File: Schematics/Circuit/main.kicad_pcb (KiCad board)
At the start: 2 copper layers, 59.3 x 59 mm, 93 parts, among them IC1 NCP1117ST33T3G, IC2 NCP1117ST50T3G, IC3 ATMEGA2560-A, IC4 RFM69HW, J1 Conn_01x03, J10 Conn_01x04, J2 Conn_01x07, J3 Conn_01x07, J4 Conn_01x07, J5 Conn_01x07, J6 Conn_01x07, J7 Conn_01x05, J8 Conn_02x05_Counter_Clockwise, J9 Conn_01x06, K1 HESOP1, K2 HESOP1, P1 CONN_2, P10 CONN_2, P11 CONN_2, P12 CONN_2, P13 CONN_2, P14 CONN_2, P15 CONN_2, P16 CONN_2, P17 CONN_2, P18 CONN_3X2, P19 CONN_O2, P2 CONN_2, P20 CONN_2, P21 CONN_2, P3 CONN_2, P4 CONN_2, P5 CONN_2, P6 CONN_2, P7 CONN_2, P8 CONN_2, P9 CONN_2, Q1 BSS138, Q2 BSS138, Q3 BSS138, Q4 BSS138, Q5 BSS138, Q6 BSS138

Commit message: Edit pcb and model
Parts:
- added J11: Conn_01x04, CanSat:MOLEX_PicoBlade_4, F.Cu at (245.9, 86.1)
- moved R15 0.42 mm to (250.7, 97.4)
- moved R24 0.15 mm to (242.5, 100.1)
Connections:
- IC3 pad 12: /RX -> /TXD-GSM
- IC3 pad 13: /TX -> /RXD-GSM
- IC3 pad 2: /TXD-GSM -> /RX
- IC3 pad 27: (no net) -> Net-(IC3-Pad27)
- IC3 pad 28: (no net) -> Net-(IC3-Pad28)
- IC3 pad 29: (no net) -> Net-(IC3-Pad29)
- IC3 pad 3: /RXD-GSM -> /TX
- IC3 pad 35: (no net) -> Net-(IC3-Pad35)
- IC3 pad 36: (no net) -> Net-(IC3-Pad36)
- IC3 pad 4: (no net) -> Net-(IC3-Pad4)
- IC3 pad 41: (no net) -> Net-(IC3-Pad41)
- IC3 pad 42: (no net) -> Net-(IC3-Pad42)
- IC3 pad 46: (no net) -> Net-(IC3-Pad46)
- IC3 pad 48: (no net) -> Net-(IC3-Pad48)
- IC3 pad 5: (no net) -> Net-(IC3-Pad5)
- IC3 pad 51: (no net) -> Net-(IC3-Pad51)
- IC3 pad 52: (no net) -> Net-(IC3-Pad52)
- IC3 pad 53: (no net) -> Net-(IC3-Pad53)
- IC3 pad 54: (no net) -> Net-(IC3-Pad54)
- IC3 pad 57: (no net) -> Net-(IC3-Pad57)
- IC3 pad 58: (no net) -> Net-(IC3-Pad58)
- IC3 pad 60: (no net) -> Net-(IC3-Pad60)
- IC3 pad 63: (no net) -> /RX_GPS
- IC3 pad 64: (no net) -> /TX_GPS
- IC3 pad 65: (no net) -> Net-(IC3-Pad65)
- IC3 pad 66: (no net) -> Net-(IC3-Pad66)
- IC3 pad 67: (no net) -> Net-(IC3-Pad67)
- IC3 pad 69: (no net) -> Net-(IC3-Pad69)
- IC3 pad 70: (no net) -> Net-(IC3-Pad70)
- IC3 pad 77: (no net) -> Net-(IC3-Pad77)
- IC3 pad 78: (no net) -> Net-(IC3-Pad78)
- IC3 pad 79: (no net) -> Net-(IC3-Pad79)
- IC3 pad 82: (no net) -> Net-(IC3-Pad82)
- IC3 pad 83: (no net) -> Net-(IC3-Pad83)
- IC3 pad 84: (no net) -> Net-(IC3-Pad84)
- IC3 pad 85: (no net) -> Net-(IC3-Pad85)
- IC3 pad 86: (no net) -> Net-(IC3-Pad86)
- IC3 pad 87: (no net) -> Net-(IC3-Pad87)
- IC3 pad 88: (no net) -> Net-(IC3-Pad88)
- IC3 pad 89: (no net) -> Net-(IC3-Pad89)
- IC3 pad 90: (no net) -> Net-(IC3-Pad90)
- IC3 pad 91: (no net) -> Net-(IC3-Pad91)
- IC3 pad 92: (no net) -> Net-(IC3-Pad92)
- IC3 pad 93: (no net) -> Net-(IC3-Pad93)
- IC3 pad 94: (no net) -> Net-(IC3-Pad94)
- IC3 pad 95: (no net) -> Net-(IC3-Pad95)
- IC3 pad 98: (no net) -> Net-(IC3-Pad98)
- IC4 pad 1: (no net) -> Net-(IC4-Pad1)
- IC4 pad 10: (no net) -> Net-(IC4-Pad10)
- IC4 pad 16: (no net) -> Net-(IC4-Pad16)
- IC4 pad 3: (no net) -> Net-(IC4-Pad3)
- IC4 pad 4: (no net) -> Net-(IC4-Pad4)
- IC4 pad 5: (no net) -> Net-(IC4-Pad5)
- IC4 pad 6: (no net) -> Net-(IC4-Pad6)
- IC4 pad 7: (no net) -> Net-(IC4-Pad7)
- J8 pad 1: (no net) -> /DTR
- J8 pad 6: (no net) -> Net-(J8-Pad6)
- K1 pad 3: (no net) -> Net-(K1-Pad3)
- K1 pad 4: (no net) -> Net-(K1-Pad4)
- K2 pad 3: (no net) -> Net-(K2-Pad3)
- K2 pad 4: (no net) -> Net-(K2-Pad4)
- P18 pad 4: (no net) -> Net-(P18-Pad4)
- P19 pad 3: (no net) -> Net-(P19-Pad3)
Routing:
- net +12V: track 605.0 -> 645.1 mm, vias 0 -> 3
- net /RX_GPS: track 0.00 -> 37.5 mm, vias 0 -> 2
- net /TX_GPS: track 0.00 -> 30.4 mm, vias 0 -> 2
- net +5V: track 291.3 -> 311.9 mm, vias 25 -> 28
- net GND: track 806.2 -> 792.4 mm, vias 21 -> 27
- net /TXD-GSM: track 13.4 -> 24.8 mm, vias 0 -> 2
- net Net-(J2-Pad5): track 51.5 -> 42.6 mm, vias 5 -> 3
- net /SCL: track 119.7 -> 126.5 mm, vias 9 -> 10
- net /TX: track 31.8 -> 36.6 mm
- net /LED_TOP: track 25.2 -> 20.9 mm
- net /RX: track 40.9 -> 43.4 mm
- net /RFMINT: track 30.6 -> 33.0 mm
- net Net-(IC4-Pad14): track 48.5 -> 50.8 mm
- net +3V3: track 175.7 -> 177.6 mm
- net /PWM5: track 18.1 -> 16.3 mm
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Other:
- rule trace_min: 0.203 -> 0.197

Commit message: Edit, add overall schematic, widen gaps in pcb
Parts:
- moved P21 200.9 mm to (18.0, 57.2)
- moved P10 200.8 mm to (67.5, 36.3)
- moved P9 200.8 mm to (71.9, 36.3)
- moved P12 200.7 mm to (67.4, 53.4)
- moved P11 200.7 mm to (71.8, 53.4)
- moved P5 200.6 mm to (34.7, 72.4)
- moved P6 200.6 mm to (34.7, 67.9)
- moved P13 200.3 mm to (36.0, 16.2)
- moved P14 200.3 mm to (36.0, 20.7)
- moved C1 200.2 mm to (30.5, 26.5)
- moved C10 200.2 mm to (32.5, 44.0)
- moved C11 200.2 mm to (38.3, 54.4)
- moved C12 200.2 mm to (47.7, 34.1)
- moved C13 200.2 mm to (35.6, 34.7)
- moved C14 200.2 mm to (54.5, 55.0)
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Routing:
- net +12V: track 645.1 -> 329.1 mm, vias 3 -> 2
- net GND: track 792.4 -> 821.5 mm
- net /SERVO: track 18.3 -> 17.2 mm
- net +3V3: track 177.6 -> 178.1 mm
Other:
- board size 59.3 x 59 mm -> 58.9 x 59 mm
- net class Default: clearance 0.197 -> 0.203
- rule trace_clearance: 0.197 -> 0.203
- rule trace_min: 0.197 -> 0.203

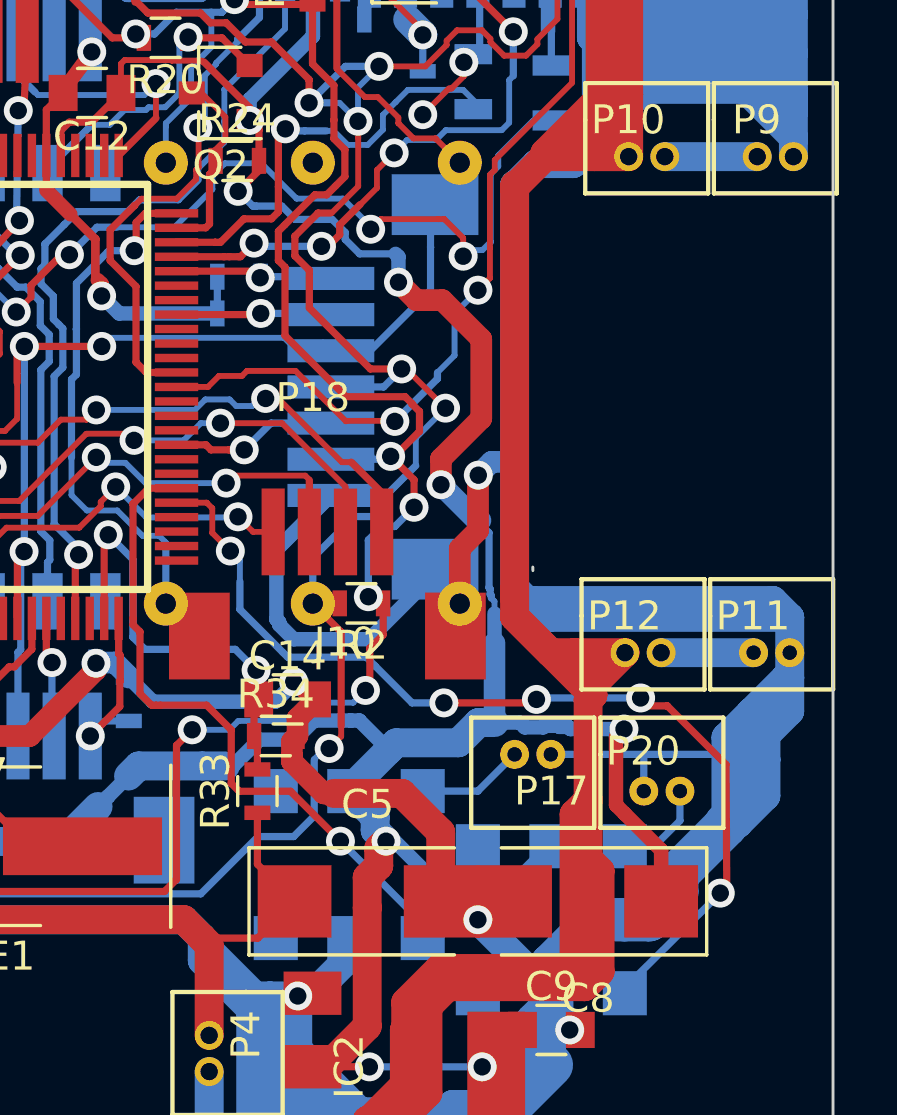
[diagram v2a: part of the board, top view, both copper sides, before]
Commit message: Edit power port distribution
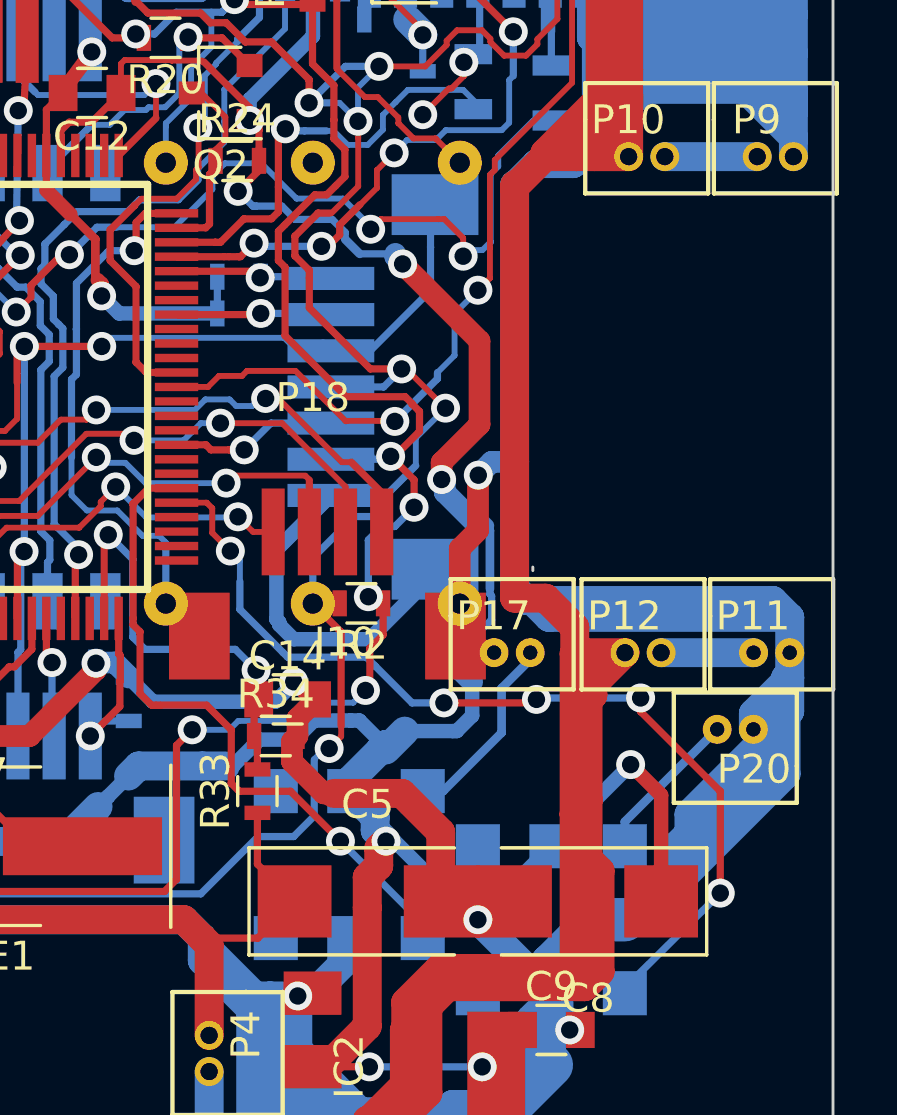
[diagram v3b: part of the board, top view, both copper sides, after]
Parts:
- moved P17 3.56 mm to (62.8, 53.4), turned to 180 degrees
- moved P20 2.49 mm to (69.3, 56.1), turned to 0 degrees
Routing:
- net /FLY_PWR: track 3.70 -> 6.82 mm
- net +5V: track 312.2 -> 309.1 mm
- net GND: track 821.5 -> 824.1 mm
- net /CAM_PWR: track 3.29 -> 5.36 mm
- net +12V: track 329.1 -> 331.0 mm

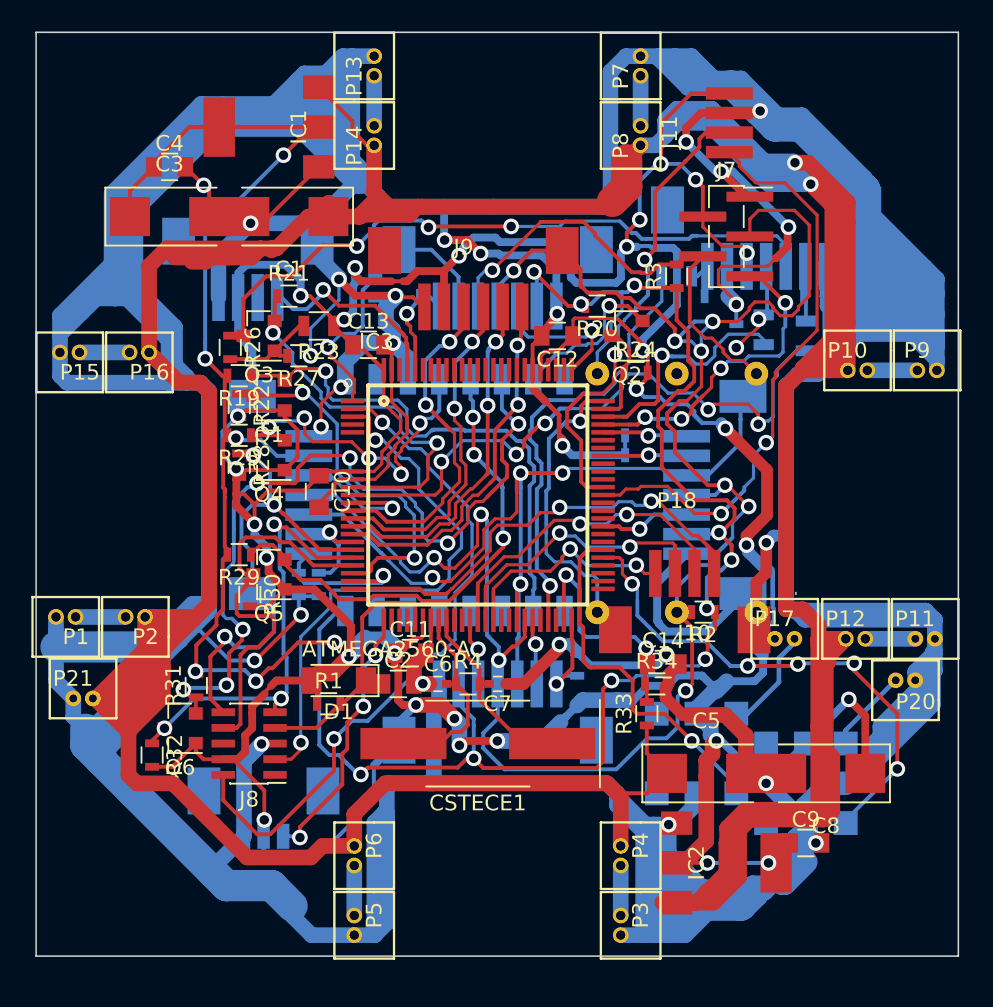
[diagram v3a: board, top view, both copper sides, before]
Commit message: Edit schematic and model, add images
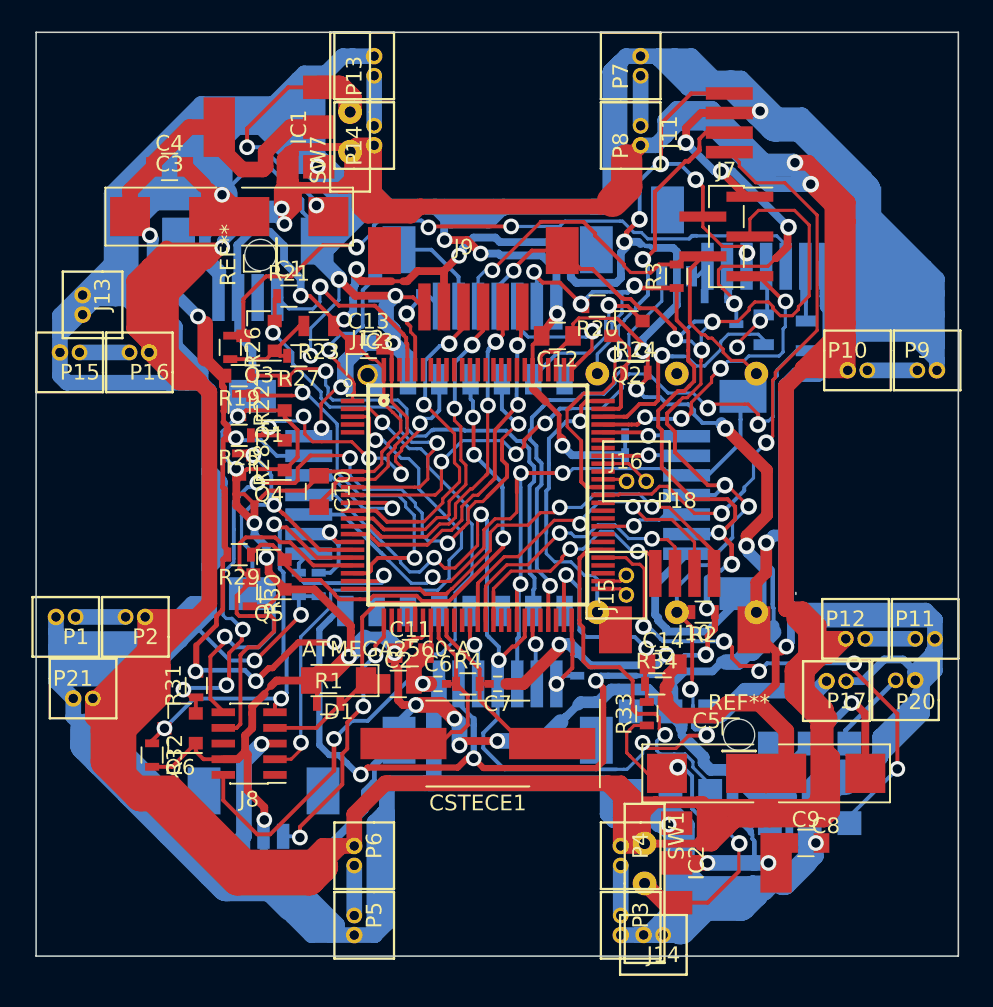
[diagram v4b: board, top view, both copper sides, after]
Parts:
- added J12: Conn_01x01, Pin_Headers:Pin_Header_Straight_1x01_Pitch2.54mm, F.Cu at (35.6, 36.6)
- added J13: Conn_01x02, CanSat:MOLEX_PicoBlade_2, F.Cu at (17.4, 32.7)
- added J14: Conn_01x02, CanSat:MOLEX_PicoBlade_2, F.Cu at (53.2, 72.3)
- added J15: Conn_01x02, CanSat:MOLEX_PicoBlade_2, F.Cu at (52.1, 49.4)
- added J16: Conn_01x02, CanSat:MOLEX_PicoBlade_2, F.Cu at (53.4, 43.4)
- added REF**: Pin_Header_Straight_1x01_Pitch2.00mm, Pin_Headers:Pin_Header_Straight_1x01_Pitch2.00mm, F.Cu at (28.7, 28.9)
- added REF**: Pin_Header_Straight_1x01_Pitch2.00mm, Pin_Headers:Pin_Header_Straight_1x01_Pitch2.00mm, F.Cu at (59.3, 59.6)
- added SW1: SW_DIP_x01, CanSat:Switch, F.Cu at (53.3, 69.1)
- added SW7: SW_DIP_x01, CanSat:Switch, F.Cu at (34.5, 19.8)
- moved P17 3.39 mm to (64.9, 56.1), turned to 0 degrees
- moved K2 1.67 mm to (54.9, 60.6)
- moved K1 0.24 mm to (63.8, 62.7)
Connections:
- C1 pad 1: +12V -> Net-(C1-Pad1)
- C5 pad 1: +12V -> Net-(C5-Pad1)
- IC1 pad 3: +12V -> Net-(C1-Pad1)
- IC2 pad 3: +12V -> Net-(C5-Pad1)
- IC3 pad 27: Net-(IC3-Pad27) -> (no net)
- IC3 pad 28: Net-(IC3-Pad28) -> (no net)
- IC3 pad 29: Net-(IC3-Pad29) -> (no net)
- IC3 pad 35: Net-(IC3-Pad35) -> (no net)
- IC3 pad 36: Net-(IC3-Pad36) -> (no net)
- IC3 pad 4: Net-(IC3-Pad4) -> (no net)
- IC3 pad 41: Net-(IC3-Pad41) -> (no net)
- IC3 pad 42: Net-(IC3-Pad42) -> (no net)
- IC3 pad 46: Net-(IC3-Pad46) -> (no net)
- IC3 pad 48: Net-(IC3-Pad48) -> (no net)
- IC3 pad 5: Net-(IC3-Pad5) -> (no net)
- IC3 pad 53: Net-(IC3-Pad53) -> (no net)
- IC3 pad 54: Net-(IC3-Pad54) -> (no net)
- IC3 pad 57: Net-(IC3-Pad57) -> (no net)
- IC3 pad 58: Net-(IC3-Pad58) -> (no net)
- IC3 pad 60: Net-(IC3-Pad60) -> (no net)
- IC3 pad 66: Net-(IC3-Pad66) -> (no net)
- IC3 pad 69: Net-(IC3-Pad69) -> (no net)
- IC3 pad 70: Net-(IC3-Pad70) -> (no net)
- IC3 pad 77: Net-(IC3-Pad77) -> (no net)
- IC3 pad 78: Net-(IC3-Pad78) -> (no net)
- IC3 pad 79: Net-(IC3-Pad79) -> (no net)
- IC3 pad 82: Net-(IC3-Pad82) -> (no net)
- IC3 pad 83: Net-(IC3-Pad83) -> (no net)
- IC3 pad 84: Net-(IC3-Pad84) -> (no net)
- IC3 pad 85: Net-(IC3-Pad85) -> (no net)
- IC3 pad 86: Net-(IC3-Pad86) -> (no net)
- IC3 pad 87: Net-(IC3-Pad87) -> (no net)
- IC3 pad 88: Net-(IC3-Pad88) -> (no net)
- IC3 pad 89: Net-(IC3-Pad89) -> (no net)
- IC3 pad 90: Net-(IC3-Pad90) -> (no net)
- IC3 pad 91: Net-(IC3-Pad91) -> (no net)
- IC3 pad 92: Net-(IC3-Pad92) -> (no net)
- IC3 pad 93: Net-(IC3-Pad93) -> (no net)
- IC3 pad 94: Net-(IC3-Pad94) -> (no net)
- IC3 pad 95: Net-(IC3-Pad95) -> (no net)
- IC3 pad 98: Net-(IC3-Pad98) -> (no net)
- IC4 pad 1: Net-(IC4-Pad1) -> (no net)
- IC4 pad 16: Net-(IC4-Pad16) -> (no net)
- IC4 pad 3: Net-(IC4-Pad3) -> (no net)
- IC4 pad 4: Net-(IC4-Pad4) -> (no net)
- IC4 pad 5: Net-(IC4-Pad5) -> (no net)
- IC4 pad 6: Net-(IC4-Pad6) -> (no net)
- IC4 pad 7: Net-(IC4-Pad7) -> (no net)
- J8 pad 1: /DTR -> (no net)
- J8 pad 6: Net-(J8-Pad6) -> (no net)
- K1 pad 3: Net-(K1-Pad3) -> (no net)
- K1 pad 4: Net-(K1-Pad4) -> (no net)
- K2 pad 3: Net-(K2-Pad3) -> (no net)
- K2 pad 4: Net-(K2-Pad4) -> (no net)
- P18 pad 4: Net-(P18-Pad4) -> (no net)
- P19 pad 3: Net-(P19-Pad3) -> (no net)
- R33 pad 1: +12V -> Net-(C5-Pad1)
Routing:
- net GND: track 824.1 -> 968.5 mm
- net +12V: track 331.0 -> 432.7 mm, vias 2 -> 5
- net Net-(C5-Pad1): track 0.00 -> 24.9 mm, vias 0 -> 2
- net Net-(C1-Pad1): track 0.00 -> 17.9 mm, vias 0 -> 2
- net +5V: track 309.1 -> 320.5 mm, vias 28 -> 27
- net Net-(IC3-Pad67): track 0.00 -> 3.22 mm
- net /SCL: track 126.6 -> 129.2 mm, vias 10 -> 12
- net /CAM_TRIG: track 33.6 -> 35.4 mm
- net +3V3: track 178.1 -> 176.4 mm
- net /SDA: track 89.1 -> 90.8 mm
- net Net-(IC3-Pad51): track 0.00 -> 1.64 mm
- net Net-(IC3-Pad52): track 0.00 -> 1.64 mm
- net Net-(IC3-Pad65): track 0.00 -> 1.56 mm
- net /FLY_PWR: track 6.82 -> 8.17 mm
- net /PWM7: track 21.9 -> 23.0 mm
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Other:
- net class Default: via_dia 1 -> 1.006
- rule via_min_size: 1 -> 1.006
